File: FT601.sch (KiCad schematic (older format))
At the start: 23 parts, among them U1 FT601, U2 ESD7016, U4 ECP5, U5 Si5351, X1 GSB443133HR, Y1 FL3000027, Y2 ABM11-141-26.000MHZ

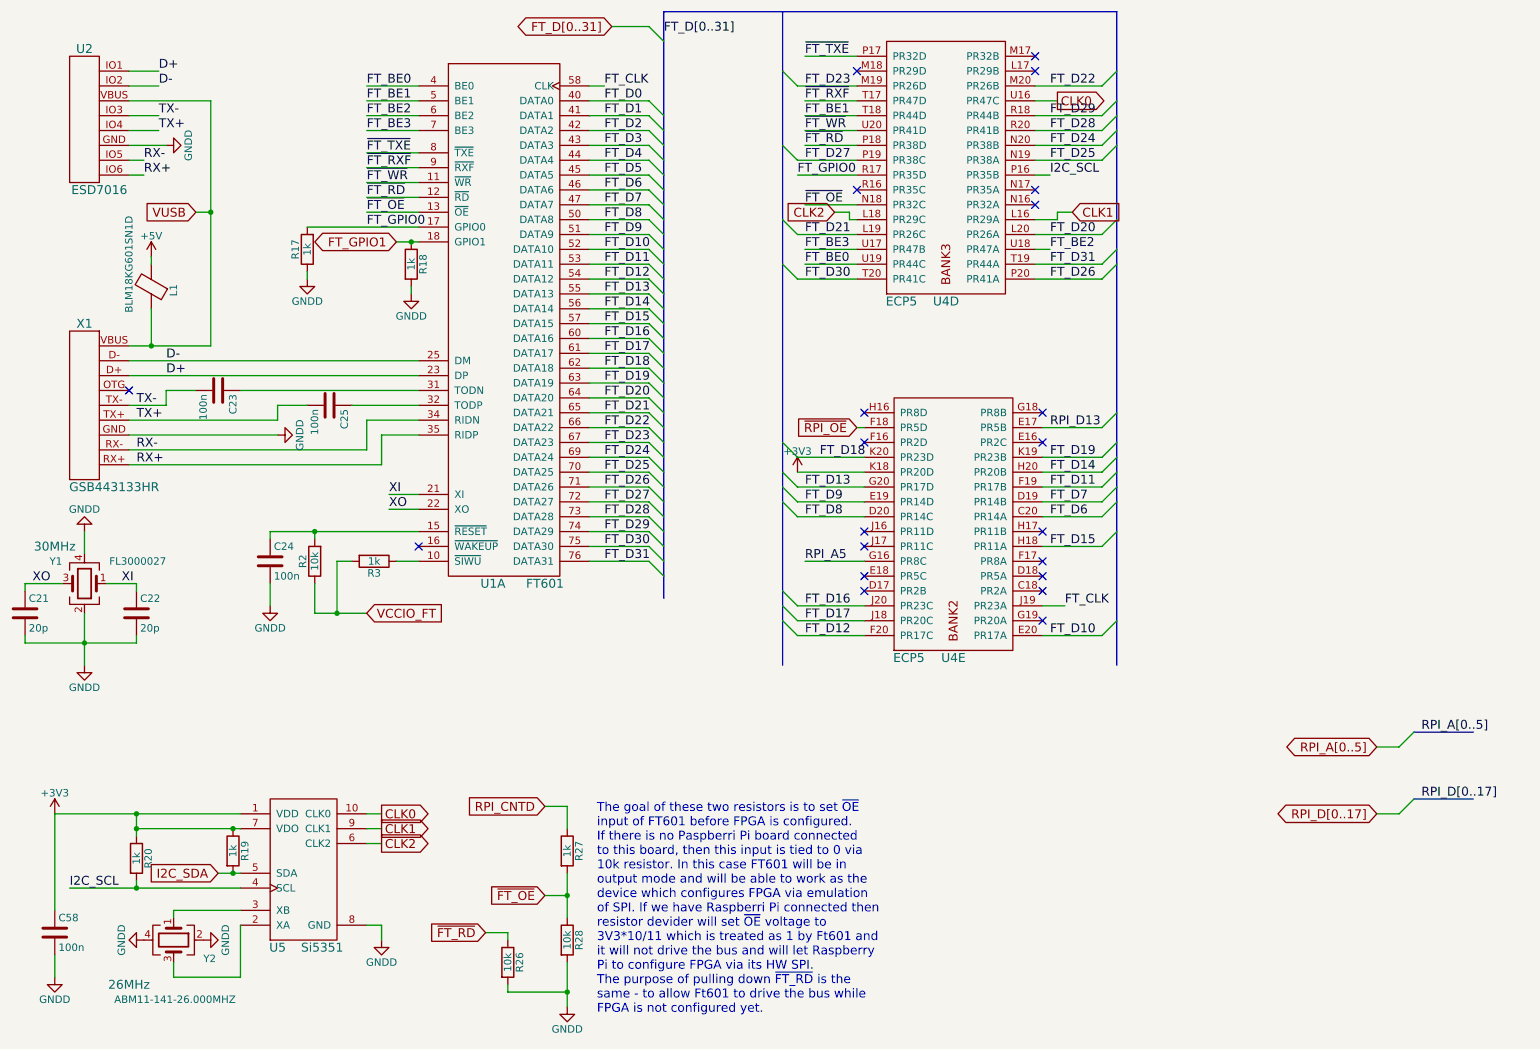
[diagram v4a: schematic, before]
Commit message: Prepared BOM and changed some part numbers for unpopular ones. Added manufacture PN for each part.
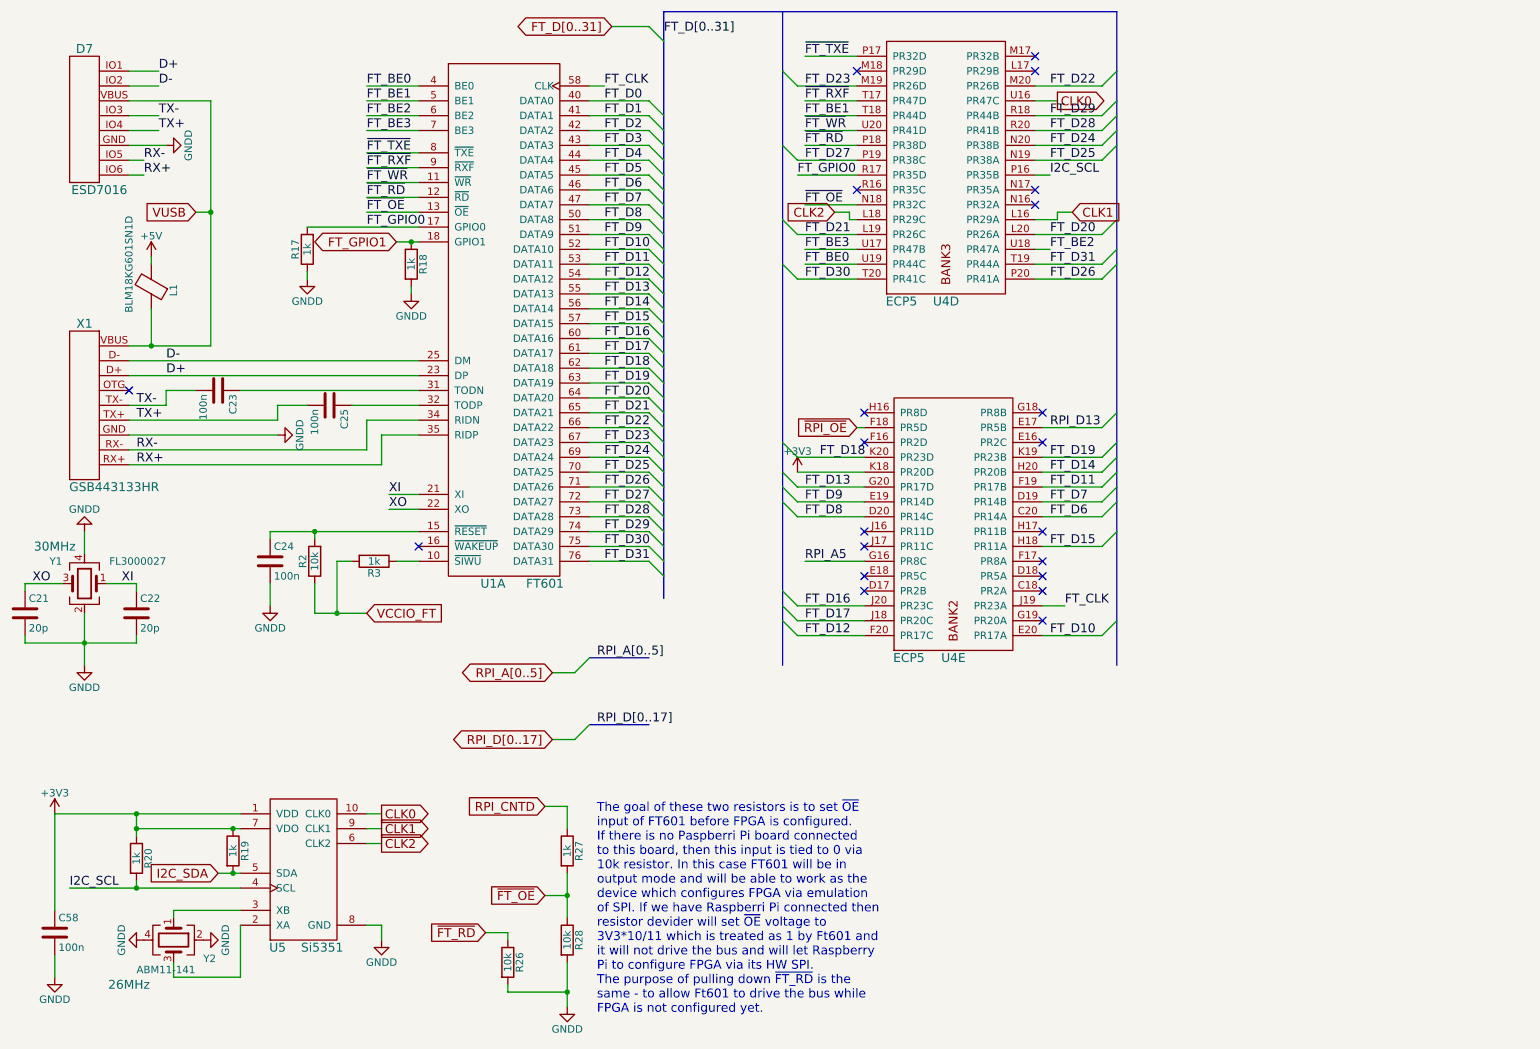
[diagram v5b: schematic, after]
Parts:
- D7: renamed from U2; manf# (none) -> ESD7016MUTAG
- L1: manf# (none) -> BLM18KG601SN1D
- R2: manf# (none) -> RC0603JR-0710KL
- R3: manf# (none) -> RC0603JR-071KL
- U1: manf# (none) -> FT601Q-B-T
- U5: manf# (none) -> SI5351A-B-GT
- X1: manf# (none) -> GSB443133HR
- Y1: manf# (none) -> FL3000027
- Y2: value ABM11-141-26.000MHZ -> ABM11-141; manf# (none) -> ABM11-141-26.000MHZ-T3
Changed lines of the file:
@@
 LIBS:valves
 LIBS:sdr
-LIBS:usb-type-c
 LIBS:sdr-cache
 EELAYER 25 0
@@
 F 2 "sdr-foots:QFN_76" H 4100 8400 60  0001 C CNN
 F 3 "" H 4100 8400 60  0001 C CNN
+F 4 "FT601Q-B-T" H 3700 4600 60  0001 C CNN "manf#"
 	1    3700 4600
 	1    0    0    -1
@@
 F 2 "sdr-foots:USB3_microB" H 1800 3050 60  0001 C CNN
 F 3 "" H 1800 3050 60  0001 C CNN
+F 4 "GSB443133HR" H 1150 2950 60  0001 C CNN "manf#"
 	1    1150 2950
 	1    0    0    -1
@@
 F 2 "Inductors_SMD:L_0805" V 1630 2650 50  0001 C CNN
 F 3 "" H 1700 2650 50  0000 C CNN
+F 4 "BLM18KG601SN1D" H 1700 2650 60  0001 C CNN "manf#"
 	1    1700 2650
 	-1   0    0    1
@@
 VUSB
 $Comp
-L ESD7016 U2
+L ESD7016 D7
 U 1 1 58980AD2
 P 1600 1050
-F 0 "U2" H 1250 1050 60  0000 C CNN
+F 0 "D7" H 1250 1050 60  0000 C CNN
 F 1 "ESD7016" H 1350 100 60  0000 C CNN
 F 2 "sdr-foots:ESD7016" H 1600 1050 60  0001 C CNN
 F 3 "" H 1600 1050 60  0001 C CNN
+F 4 "ESD7016MUTAG" H 1600 1050 60  0001 C CNN "manf#"
 	1    1600 1050
 	1    0    0    -1
@@
 F 2 "Resistors_SMD:R_0603" V 3130 4500 50  0001 C CNN
 F 3 "" H 3200 4500 50  0000 C CNN
+F 4 "RC0603JR-071KL" H 3200 4500 60  0001 C CNN "manf#"
 	1    3200 4500
 	0    1    1    0
@@
 F 2 "Resistors_SMD:R_0603" V 2730 4500 50  0001 C CNN
 F 3 "" H 2800 4500 50  0000 C CNN
+F 4 "RC0603JR-0710KL" H 2800 4500 60  0001 C CNN "manf#"
 	1    2800 4500
 	-1   0    0    1
@@
 F 2 "Crystals:Crystal_SMD_3225-4pin_3.2x2.5mm" H 1250 4650 50  0001 C CNN
 F 3 "" H 1250 4650 50  0000 C CNN
-F 4 "30MHz" H 1450 4400 60  0000 C CNN "Frequency"
+F 4 "FL3000027" H 1250 4650 60  0001 C CNN "manf#"
+F 5 "30MHz" H 1450 4400 60  0000 C CNN "Frequency"
 	1    1250 4650
 	-1   0    0    1
@@
 F 2 "Housings_SSOP:MSOP-10_3x3mm_Pitch0.5mm" H 1350 6650 60  0001 C CNN
 F 3 "" H 1350 6650 60  0001 C CNN
+F 4 "SI5351A-B-GT" H 2500 7050 60  0001 C CNN "manf#"
 	1    2500 7050
 	1    0    0    -1
@@
 P 1850 7050
 F 0 "Y2" V 1975 7250 50  0000 L CNN
-F 1 "ABM11-141-26.000MHZ" V 2250 6650 50  0000 L CNN
+F 1 "ABM11-141" V 2050 6800 50  0000 L CNN
 F 2 "Crystals:Crystal_SMD_2016-4pin_2.0x1.6mm" H 1850 7050 50  0001 C CNN
 F 3 "" H 1850 7050 50  0000 C CNN
-F 4 "26MHz" V 2150 6750 60  0000 C CNN "Frequency"
+F 4 "ABM11-141-26.000MHZ-T3" H 1850 7050 60  0001 C CNN "manf#"
+F 5 "26MHz" V 2150 6750 60  0000 C CNN "Frequency"
 	1    1850 7050
 	0    1    1    0
@@
 Text Label 7750 3600 0    60   ~ 0
 RPI_D13
-Text GLabel 9950 6200 0    60   BiDi ~ 0
+Text GLabel 4400 5700 0    60   BiDi ~ 0
 RPI_D[0..17]
 Entry Wire Line
-	10100 6200 10200 6100
-Text Label 10250 6100 0    60   ~ 0
+	4550 5700 4650 5600
+Text Label 4700 5600 0    60   ~ 0
 RPI_D[0..17]
 Entry Wire Line
 	8100 3600 8200 3500
-Text GLabel 9950 5750 0    60   BiDi ~ 0
+Text GLabel 4400 5250 0    60   BiDi ~ 0
 RPI_A[0..5]
 Entry Wire Line
-	10100 5750 10200 5650
-Text Label 10250 5650 0    60   ~ 0
+	4550 5250 4650 5150
+Text Label 4700 5150 0    60   ~ 0
 RPI_A[0..5]
 Text Label 6100 4500 0    60   ~ 0
@@
 	6400 2200 6450 2200
 Wire Wire Line
-	10100 6200 9950 6200
+	4550 5700 4400 5700
 Wire Bus Line
-	10200 6100 10600 6100
+	4650 5600 5050 5600
 Wire Wire Line
 	7700 3600 8100 3600
 Wire Wire Line
-	10100 5750 9950 5750
+	4550 5250 4400 5250
 Wire Bus Line
-	10200 5650 10600 5650
+	4650 5150 5050 5150
 Wire Wire Line
 	6100 4500 6500 4500
